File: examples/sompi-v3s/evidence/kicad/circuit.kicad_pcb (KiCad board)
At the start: 6 copper layers, 90 x 60 mm, 132 parts, among them J1 USB-C 16P, J2 RJ45 HR911105A, J3 microSD, J4 LCD 40P RGB, J5 CAM MIPI 24P, J6 3.5mm jack, J7 GPIO 2x13, J8 UART0 debug, Q1 AO3400A, SW1 RESET, SW2 KEY1, U1 Allwinner V3s, U2 TPS562200, U3 TPS562200, U4 ME6211C18M5G, U5 XC6206P302MR, U6 W25Q128JVSIQ, U8 USBLC6-2SC6, Y1 24MHz, Y2 32.768kHz

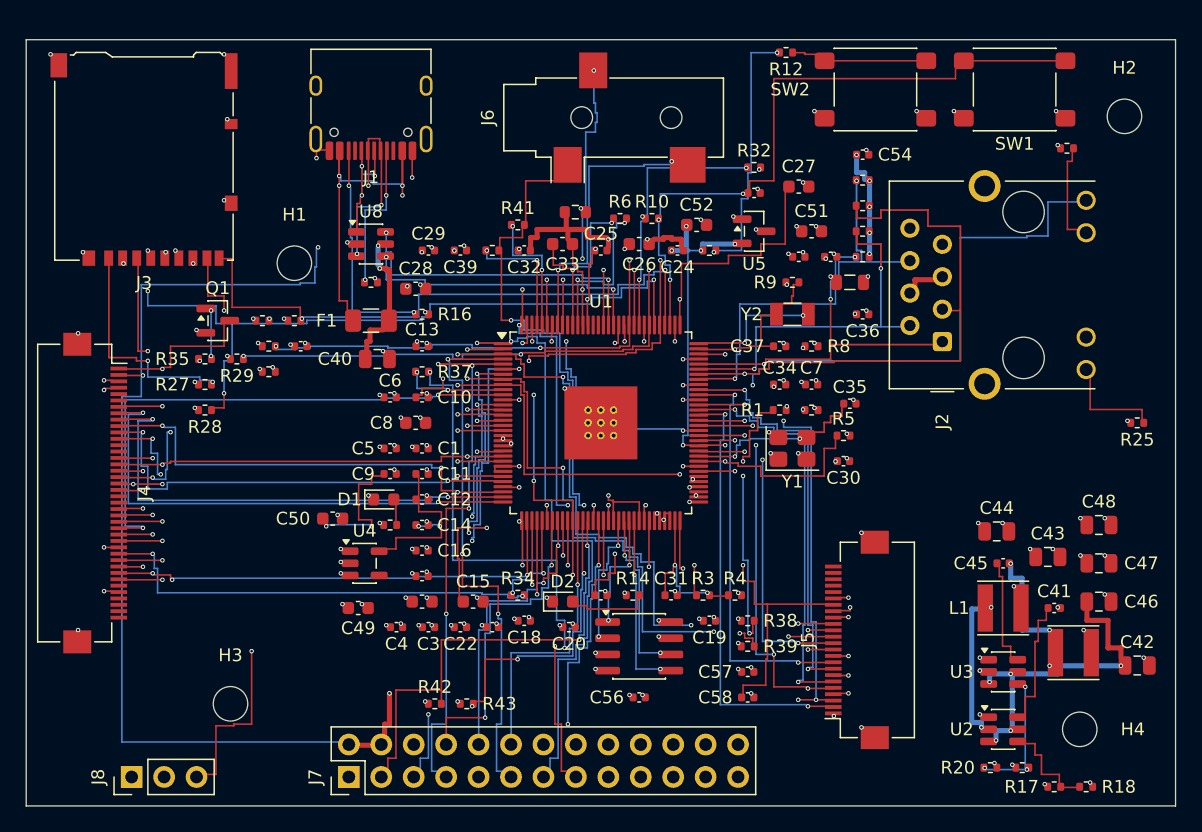
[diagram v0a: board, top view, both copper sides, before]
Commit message: evidence: SomPi-V3s rebuilt with someda 0.7.0 — 7 of 7 pairs coupled within skew budget, 0 crosstalk violations, kicad-cli DRC 0 errors, 6/6 gates
Co-Authored-By: Claude Fable 5.1 <noreply@anthropic.com>
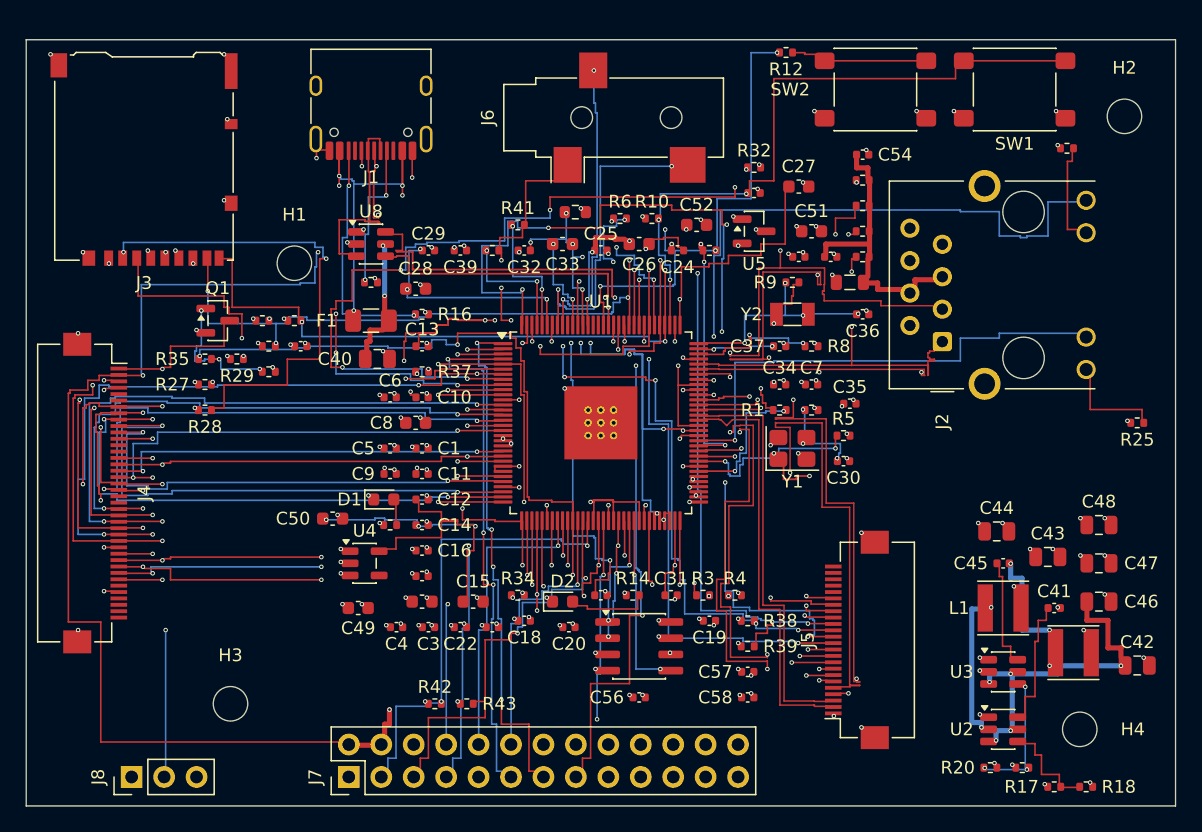
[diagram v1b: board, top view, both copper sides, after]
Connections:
- J5 pad 2: CAM_MCSI_D0N -> CAM_MCSI_D0P
- J5 pad 3: CAM_MCSI_D0P -> CAM_MCSI_D0N
- J5 pad 5: CAM_MCSI_D1N -> CAM_MCSI_D1P
- J5 pad 6: CAM_MCSI_D1P -> CAM_MCSI_D1N
- J5 pad 8: CAM_MCSI_CKN -> CAM_MCSI_CKP
- J5 pad 9: CAM_MCSI_CKP -> CAM_MCSI_CKN
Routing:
- net CAM_SDA: track 50.0 -> 111.5 mm, vias 5 -> 8
- net GPIO_PG5: track 43.8 -> 89.5 mm, vias 4 -> 6
- net +1V8: track 138.4 -> 180.3 mm, vias 19 -> 24
- net CAM_SCL: track 49.0 -> 81.7 mm, vias 5 -> 8
- net X24M_IN: track 13.2 -> 28.7 mm, vias 3 -> 4
- net CAM_MCSI_D1P: track 32.4 -> 45.7 mm
- net CAM_MCSI_D1N: track 33.0 -> 45.4 mm
- net SD_D3: track 61.1 -> 70.9 mm
- net ETH_TXN: track 28.1 -> 37.2 mm, vias 2 -> 3
- net LCD_PE4: track 44.6 -> 53.6 mm, vias 3 -> 4
- net ETH_RXN: track 31.5 -> 40.1 mm, vias 2 -> 4
- net LRADC0: track 48.4 -> 56.9 mm, vias 4 -> 5
- net LCD_PE18: track 39.5 -> 47.8 mm
- net +1V2: track 21.7 -> 30.0 mm, vias 24 -> 22
- net CAM_MCSI_CKP: track 31.8 -> 39.9 mm, vias 2 -> 4
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
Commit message: feat: fetch-libs step, repair-loop and connector-orientation contract, SomPi evidence rebuilt (someda 1d11b951fee7)
- scripts/fetch-libs.py + setup_libraries: KiCad GitLab, LCSC/EasyEDA by lcsc or mpn
  (JLCPCB parts search), vendor zip import; every part ends FOUND / FETCHED / MISSING
- SKILL.md, pcb-plan.md, pcb-build.md, CONTRACT.md: schematic approval -> fetch-libs ->
  build with the engine's repair rounds (SOMEDA_REPAIR_ROUNDS, repair:/suggest: lines,
  plan.built.json); edge_overhang_mm and engine-derived connector rotations; placement
  order and island growth documented
- examples/sompi-v3s: plan without connector rotations (the engine orients), pairs, part
  numbers; evidence of the final 0.7.0 build: 187/187 routed, 7/7 pairs within skew
  budget, 0 crosstalk violations, kicad-cli DRC 0 errors, all six gates, schematic
  PDF/SVG, 3D renders, detailed BOM, JLCPCB order package

Co-Authored-By: Claude Fable 5.1 <noreply@anthropic.com>
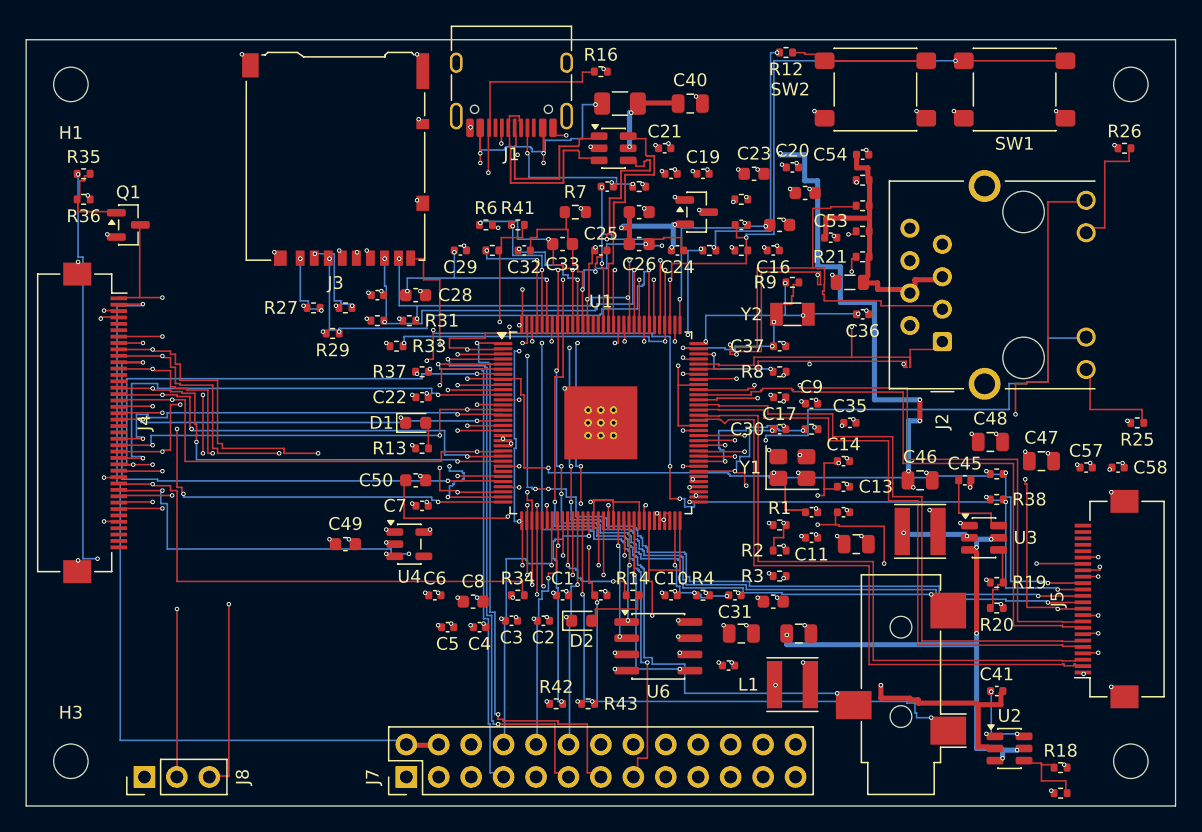
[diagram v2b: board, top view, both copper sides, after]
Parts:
- moved J6 49.8 mm to (68.5, 50.5), turned to 180 degrees
- moved C23 42.4 mm to (57.0, 10.5)
- moved C20 40.0 mm to (60.0, 10.0)
- moved C21 39.9 mm to (50.0, 8.50)
- moved C18 36.8 mm to (50.5, 10.5)
- moved C16 36.2 mm to (58.5, 16.5)
- moved C19 35.0 mm to (53.0, 10.5)
- moved C2 34.8 mm to (40.5, 45.5)
- moved C13 34.8 mm to (64.0, 35.0)
- moved C58 34.1 mm to (85.5, 33.5)
- moved C9 33.5 mm to (61.5, 28.5)
- moved C14 33.4 mm to (64.0, 33.0)
- moved C12 33.0 mm to (64.0, 37.0)
- moved C7 31.9 mm to (31.0, 36.5)
- moved C40 31.6 mm to (52.0, 5.00)
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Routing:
- net +1V8: track 180.3 -> 92.6 mm, vias 24 -> 22
- net CAM_SDA: track 111.5 -> 63.9 mm, vias 8 -> 4
- net GPIO_PG5: track 89.5 -> 48.5 mm, vias 6 -> 4
- net SD_D3: track 70.9 -> 35.7 mm, vias 4 -> 3
- net HP_R: track 23.6 -> 54.5 mm, vias 2 -> 3
- net HP_L: track 24.3 -> 54.2 mm, vias 2 -> 5
- net HPCOM_OUT: track 45.5 -> 73.4 mm, vias 5 -> 7
- net VBUS: track 169.3 -> 195.5 mm, vias 10 -> 14
- net BL_PWM: track 50.3 -> 74.0 mm
- net CAM_PWDN: track 54.0 -> 76.7 mm, vias 3 -> 6
- net SD_D2: track 61.6 -> 40.9 mm, vias 4 -> 3
- net SD_CLK: track 53.6 -> 35.1 mm
- net SD_D1: track 46.9 -> 28.4 mm
- net X24M_IN: track 28.7 -> 10.7 mm, vias 4 -> 2
- net CAM_MCSI_D0P: track 32.5 -> 48.9 mm
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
